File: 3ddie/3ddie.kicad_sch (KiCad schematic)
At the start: 53 parts, among them J1 USB4105-GF-A, J2 TRS_MIDI_IN, J3 TRS_MIDI_OUT, U1 W25Q128JV, U2 RP2040, U3 MCP1702T-3302E_CB, U4 MGC3130-I/MQ, U5 MCP1416R, U6 6N137, U7 BoostedElectrodes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

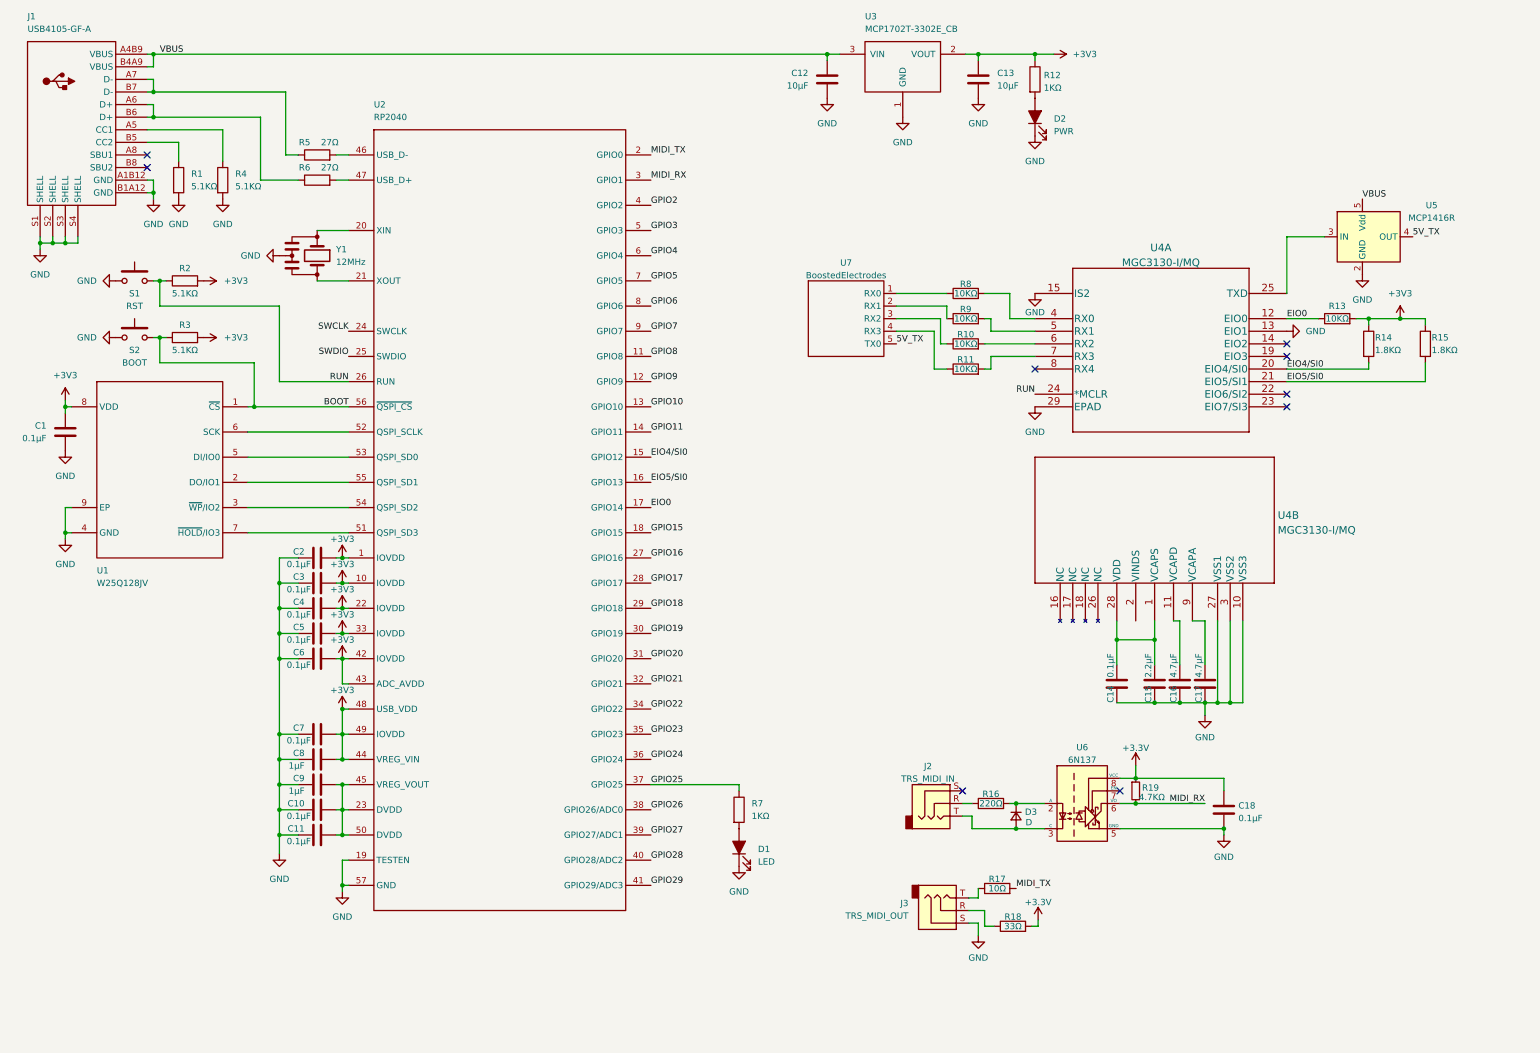
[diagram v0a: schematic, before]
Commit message: add datasheet links, part numbers, and catalog numbers to symbols
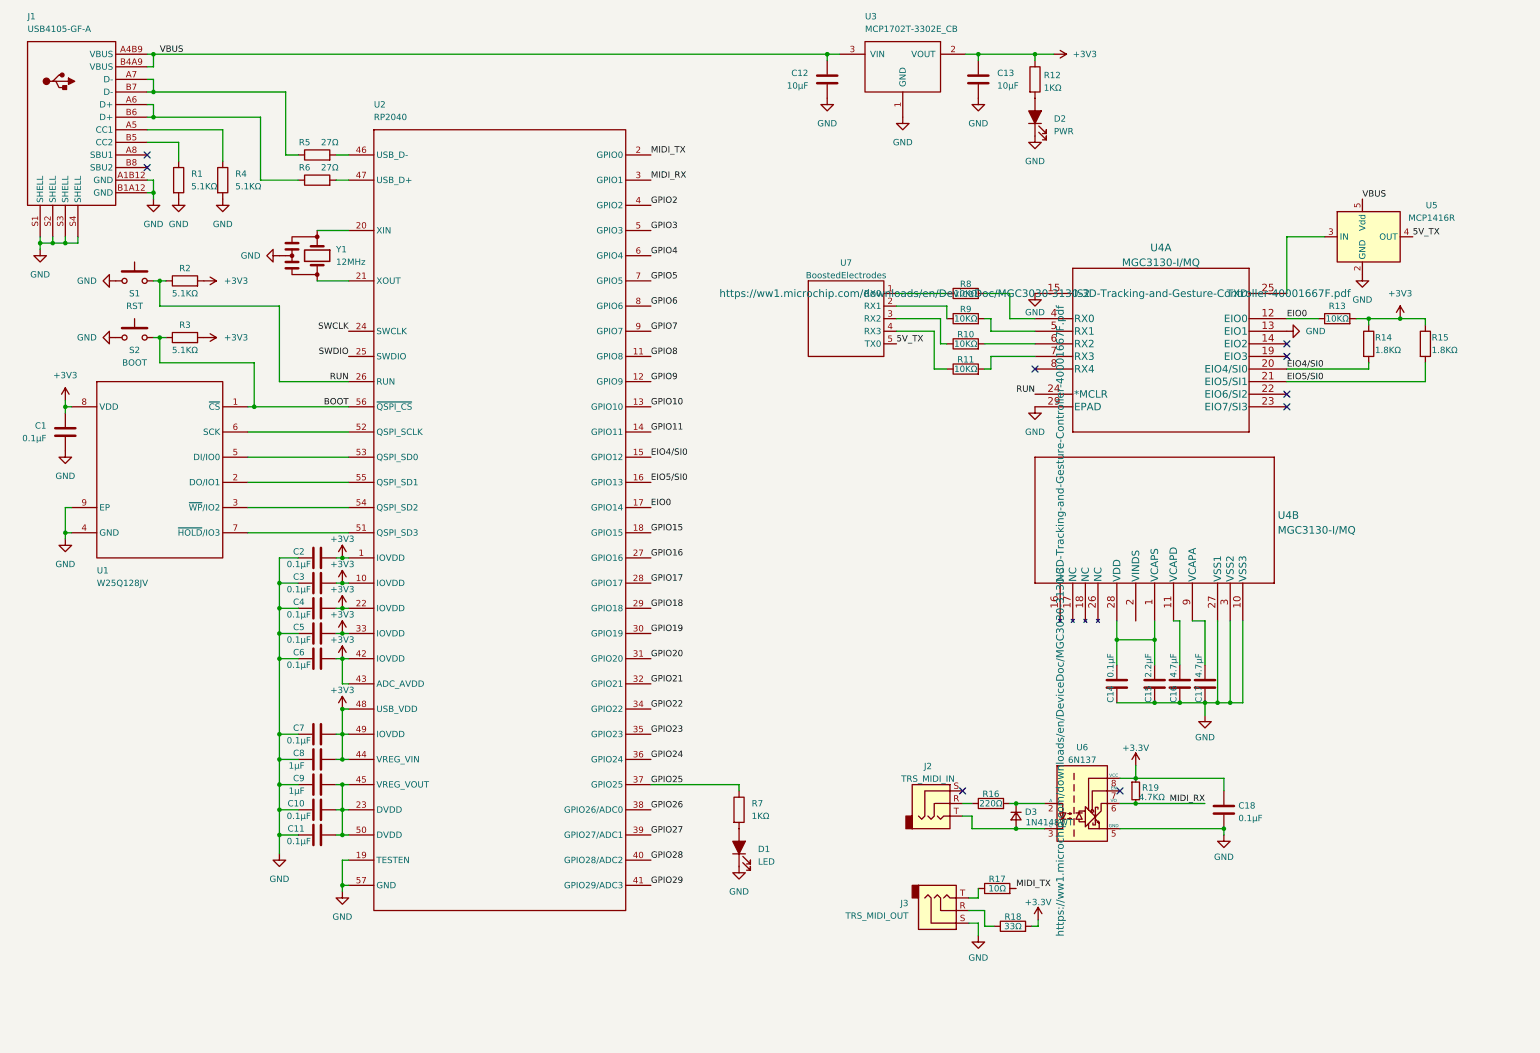
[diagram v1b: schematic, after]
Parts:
- D1: Digikey Catalog # (none) -> 160-1887-1-ND
- D2: Digikey Catalog # (none) -> 160-1427-1-ND
- D3: value D -> 1N4148WT; Digikey Catalog # (none) -> 1N4148WTCT-ND; Manufacturer Part # (none) -> 1N4148WT
- J1: Digikey Catalog # (none) -> 2073-USB4105-GF-ACT-ND; Manufacturer Part # (none) -> USB4105-GF-A
- S1, S2: Digikey Catalog # (none) -> CKN10778CT-ND; Manufacturer Part # (none) -> KTX 321 LHS
- U1: Digikey Catalog # (none) -> W25Q128JVPIMCT-ND; Manufacturer Part # (none) -> W25Q128JVPIM TR
- U2: Digikey Catalog # (none) -> 2648-SC0914(13)CT-ND; Manufacturer Part # (none) -> SC0914(13)
- U3: Digikey Catalog # (none) -> MCP1702T-3302E/CBCT-ND; Manufacturer Part # (none) -> MCP1702T-3302E/CB
- U4: Digikey Catalog # (none) -> MGC3130-I/MQ-ND; Manufacturer Part # (none) -> MGC3130-I/MQ
- U5: Digikey Catalog # (none) -> MCP1416RT-E/OTCT-ND; Manufacturer Part # (none) -> MCP1416RT-E/OT
- U6: footprint Package_DIP:DIP-8_W7.62mm -> (none); Digikey Catalog # (none) -> 6N137SM-ND; Manufacturer Part # (none) -> 6N137SM
- Y1: Digikey Catalog # (none) -> 490-17944-1-ND; Manufacturer Part # (none) -> CSTNE12M0G55A000R0
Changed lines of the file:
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@@
+      (effects (font (size 1.27 1.27)) hide)
+    )
+    (property "Digikey Catalog #" "MCP1416RT-E/OTCT-ND" (id 4) (at 292.1 66.04 0)
+      (effects (font (size 1.27 1.27)) hide)
+    )
+    (property "Manufacturer Part #" "MCP1416RT-E/OT" (id 5) (at 292.1 66.04 0)
       (effects (font (size 1.27 1.27)) hide)
     )
@@
       (effects (font (size 1.27 1.27)) hide)
     )
+    (property "Digikey Catalog #" "160-1887-1-ND" (id 4) (at 166.37 189.23 0)
+      (effects (font (size 1.27 1.27)) hide)
+    )
     (pin "1")
     (pin "2")
@@
       (effects (font (size 1.524 1.524)) hide)
     )
-    (property "Datasheet" "" (id 3) (at 231.14 143.51 0)
+    (property "Datasheet" "https://ww1.microchip.com/downloads/en/DeviceDoc/MGC3030-3130-3D-Tracking-and-Gesture-Controller-40001667F.pdf" (id 3) (at 231.14 143.51 0)
       (effects (font (size 1.524 1.524)))
+    )
+    (property "Digikey Catalog #" "MGC3130-I/MQ-ND" (id 4) (at 231.14 143.51 0)
+      (effects (font (size 1.27 1.27)) hide)
+    )
+    (property "Manufacturer Part #" "MGC3130-I/MQ" (id 5) (at 231.14 143.51 0)
+      (effects (font (size 1.27 1.27)) hide)
     )
     (pin "12")
@@
       (effects (font (size 1.27 1.27)) hide)
     )
-    (property "Datasheet" "" (id 3) (at 81.28 69.85 0)
+    (property "Datasheet" "https://www.murata.com/en/products/productdata/8801162002462/SPEC-CSTNE12M0G55A000R0.pdf" (id 3) (at 81.28 69.85 0)
+      (effects (font (size 1.27 1.27)) hide)
+    )
+    (property "Digikey Catalog #" "490-17944-1-ND" (id 4) (at 81.28 69.85 0)
+      (effects (font (size 1.27 1.27)) hide)
+    )
+    (property "Manufacturer Part #" "CSTNE12M0G55A000R0" (id 5) (at 81.28 69.85 0)
       (effects (font (size 1.27 1.27)) hide)
     )
@@
       (effects (font (size 1.524 1.524)) hide)
     )
-    (property "Datasheet" "" (id 3) (at 46.99 76.2 90)
+    (property "Datasheet" "https://www.ckswitches.com/media/1465/kxt3.pdf" (id 3) (at 46.99 76.2 90)
       (effects (font (size 1.524 1.524)) hide)
     )
+    (property "Digikey Catalog #" "CKN10778CT-ND" (id 4) (at 44.45 74.93 0)
+      (effects (font (size 1.27 1.27)) hide)
+    )
+    (property "Manufacturer Part #" "KTX 321 LHS" (id 5) (at 44.45 74.93 0)
+      (effects (font (size 1.27 1.27)) hide)
+    )
     (pin "1")
     (pin "2")
@@
       (effects (font (size 1.27 1.27)) (justify left))
     )
-    (property "Value" "D" (id 1) (at 224.155 184.15 90)
+    (property "Value" "1N4148WT" (id 1) (at 224.155 184.15 90)
       (effects (font (size 1.27 1.27)) (justify left))
     )
@@
       (effects (font (size 1.27 1.27)) hide)
     )
-    (property "Datasheet" "~" (id 3) (at 222.25 182.88 90)
+    (property "Datasheet" "https://rocelec.widen.net/view/pdf/bnxdzepaue/ONSM-S-A0003584797-1.pdf?t.download=true&u=5oefqw" (id 3) (at 222.25 182.88 90)
+      (effects (font (size 1.27 1.27)) hide)
+    )
+    (property "Digikey Catalog #" "1N4148WTCT-ND" (id 4) (at 222.25 182.88 0)
+      (effects (font (size 1.27 1.27)) hide)
+    )
+    (property "Manufacturer Part #" "1N4148WT" (id 5) (at 222.25 182.88 0)
       (effects (font (size 1.27 1.27)) hide)
     )
@@
       (effects (font (size 1.524 1.524)) hide)
     )
-    (property "Datasheet" "" (id 3) (at 46.99 87.63 90)
+    (property "Datasheet" "https://www.ckswitches.com/media/1465/kxt3.pdf" (id 3) (at 46.99 87.63 90)
       (effects (font (size 1.524 1.524)) hide)
+    )
+    (property "Digikey Catalog #" "CKN10778CT-ND" (id 4) (at 44.45 86.36 0)
+      (effects (font (size 1.27 1.27)) hide)
+    )
+    (property "Manufacturer Part #" "KTX 321 LHS" (id 5) (at 44.45 86.36 0)
+      (effects (font (size 1.27 1.27)) hide)
     )
     (pin "1")
@@
       (effects (font (size 1.524 1.524)) hide)
     )
-    (property "Datasheet" "" (id 3) (at 226.06 77.47 0)
+    (property "Datasheet" "https://ww1.microchip.com/downloads/en/DeviceDoc/MGC3030-3130-3D-Tracking-and-Gesture-Controller-40001667F.pdf" (id 3) (at 226.06 77.47 0)
       (effects (font (size 1.524 1.524)))
+    )
+    (property "Digikey Catalog #" "MGC3130-I/MQ-ND" (id 4) (at 226.06 77.47 0)
+      (effects (font (size 1.27 1.27)) hide)
+    )
+    (property "Manufacturer Part #" "MGC3130-I/MQ" (id 5) (at 226.06 77.47 0)
+      (effects (font (size 1.27 1.27)) hide)
     )
     (pin "12")
@@
     (property "Reference" "U6" (id 0) (at 235.585 169.0202 0))
     (property "Value" "6N137" (id 1) (at 235.585 171.5571 0))
-    (property "Footprint" "Package_DIP:DIP-8_W7.62mm" (id 2) (at 235.585 193.04 0)
-      (effects (font (size 1.27 1.27)) hide)
-    )
-    (property "Datasheet" "https://docs.broadcom.com/docs/AV02-0940EN" (id 3) (at 213.995 166.37 0)
+    (property "Footprint" "" (id 2) (at 235.585 193.04 0)
+      (effects (font (size 1.27 1.27)) hide)
+    )
+    (property "Datasheet" "https://rocelec.widen.net/view/pdf/zs07d29frw/ONSM-S-A0003591003-1.pdf?t.download=true&u=5oefqw" (id 3) (at 213.995 166.37 0)
+      (effects (font (size 1.27 1.27)) hide)
+    )
+    (property "Digikey Catalog #" "6N137SM-ND" (id 4) (at 235.585 180.34 0)
+      (effects (font (size 1.27 1.27)) hide)
+    )
+    (property "Manufacturer Part #" "6N137SM" (id 5) (at 235.585 180.34 0)
       (effects (font (size 1.27 1.27)) hide)
     )
@@
       (effects (font (size 1.27 1.27)) hide)
     )
+    (property "Digikey Catalog #" "160-1427-1-ND" (id 4) (at 226.06 41.91 0)
+      (effects (font (size 1.27 1.27)) hide)
+    )
     (pin "1")
     (pin "2")
@@
       (effects (font (size 1.524 1.524)) hide)
     )
-    (property "Datasheet" "" (id 3) (at 199.39 30.48 0)
+    (property "Datasheet" "https://ww1.microchip.com/downloads/en/DeviceDoc/22008E.pdf" (id 3) (at 199.39 30.48 0)
       (effects (font (size 1.524 1.524)) hide)
     )
+    (property "Digikey Catalog #" "MCP1702T-3302E/CBCT-ND" (id 4) (at 199.39 31.75 0)
+      (effects (font (size 1.27 1.27)) hide)
+    )
+    (property "Manufacturer Part #" "MCP1702T-3302E/CB" (id 5) (at 199.39 31.75 0)
+      (effects (font (size 1.27 1.27)) hide)
+    )
     (pin "1")
     (pin "2")
@@
     )
     (property "Datasheet" "" (id 3) (at 29.21 39.37 0)
+      (effects (font (size 1.27 1.27)) hide)
+    )
+    (property "Digikey Catalog #" "2073-USB4105-GF-ACT-ND" (id 4) (at 31.75 43.18 0)
+      (effects (font (size 1.27 1.27)) hide)
+    )
+    (property "Manufacturer Part #" "USB4105-GF-A" (id 5) (at 31.75 43.18 0)
       (effects (font (size 1.27 1.27)) hide)
     )
@@
       (effects (font (size 1.27 1.27)) hide)
     )
-    (property "Datasheet" "" (id 3) (at 54.61 104.14 0)
+    (property "Datasheet" "https://www.winbond.com/resource-files/w25q128jv_dtr%20revc%2003272018%20plus.pdf" (id 3) (at 54.61 104.14 0)
+      (effects (font (size 1.27 1.27)) hide)
+    )
+    (property "Digikey Catalog #" "W25Q128JVPIMCT-ND" (id 4) (at 49.53 113.03 0)
+      (effects (font (size 1.27 1.27)) hide)
+    )
+    (property "Manufacturer Part #" "W25Q128JVPIM TR" (id 5) (at 49.53 113.03 0)
       (effects (font (size 1.27 1.27)) hide)
     )
@@
       (effects (font (size 1.27 1.27)) hide)
     )
-    (property "Datasheet" "" (id 3) (at 124.46 87.63 0)
+    (property "Datasheet" "https://datasheets.raspberrypi.com/rp2040/rp2040-datasheet.pdf" (id 3) (at 124.46 87.63 0)
+      (effects (font (size 1.27 1.27)) hide)
+    )
+    (property "Digikey Catalog #" "2648-SC0914(13)CT-ND" (id 4) (at 118.11 123.19 0)
+      (effects (font (size 1.27 1.27)) hide)
+    )
+    (property "Manufacturer Part #" "SC0914(13)" (id 5) (at 118.11 123.19 0)
       (effects (font (size 1.27 1.27)) hide)
     )
@@
     )
     (path "/6c8f9fa6-c3d2-4a4b-a5e3-d21e80be9063"
-      (reference "D3") (unit 1) (value "D") (footprint "")
+      (reference "D3") (unit 1) (value "1N4148WT") (footprint "")
     )
     (path "/e852571c-5d4c-418a-a34d-71f60de57e95"
@@
     )
     (path "/bca2ac86-8d9c-4b32-ab1d-2258827622a1"
-      (reference "U6") (unit 1) (value "6N137") (footprint "Package_DIP:DIP-8_W7.62mm")
+      (reference "U6") (unit 1) (value "6N137") (footprint "")
     )
     (path "/0030390e-c97e-47e6-97d2-f7c983a931fc"

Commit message: specify optocoupler diode, assign some footprints
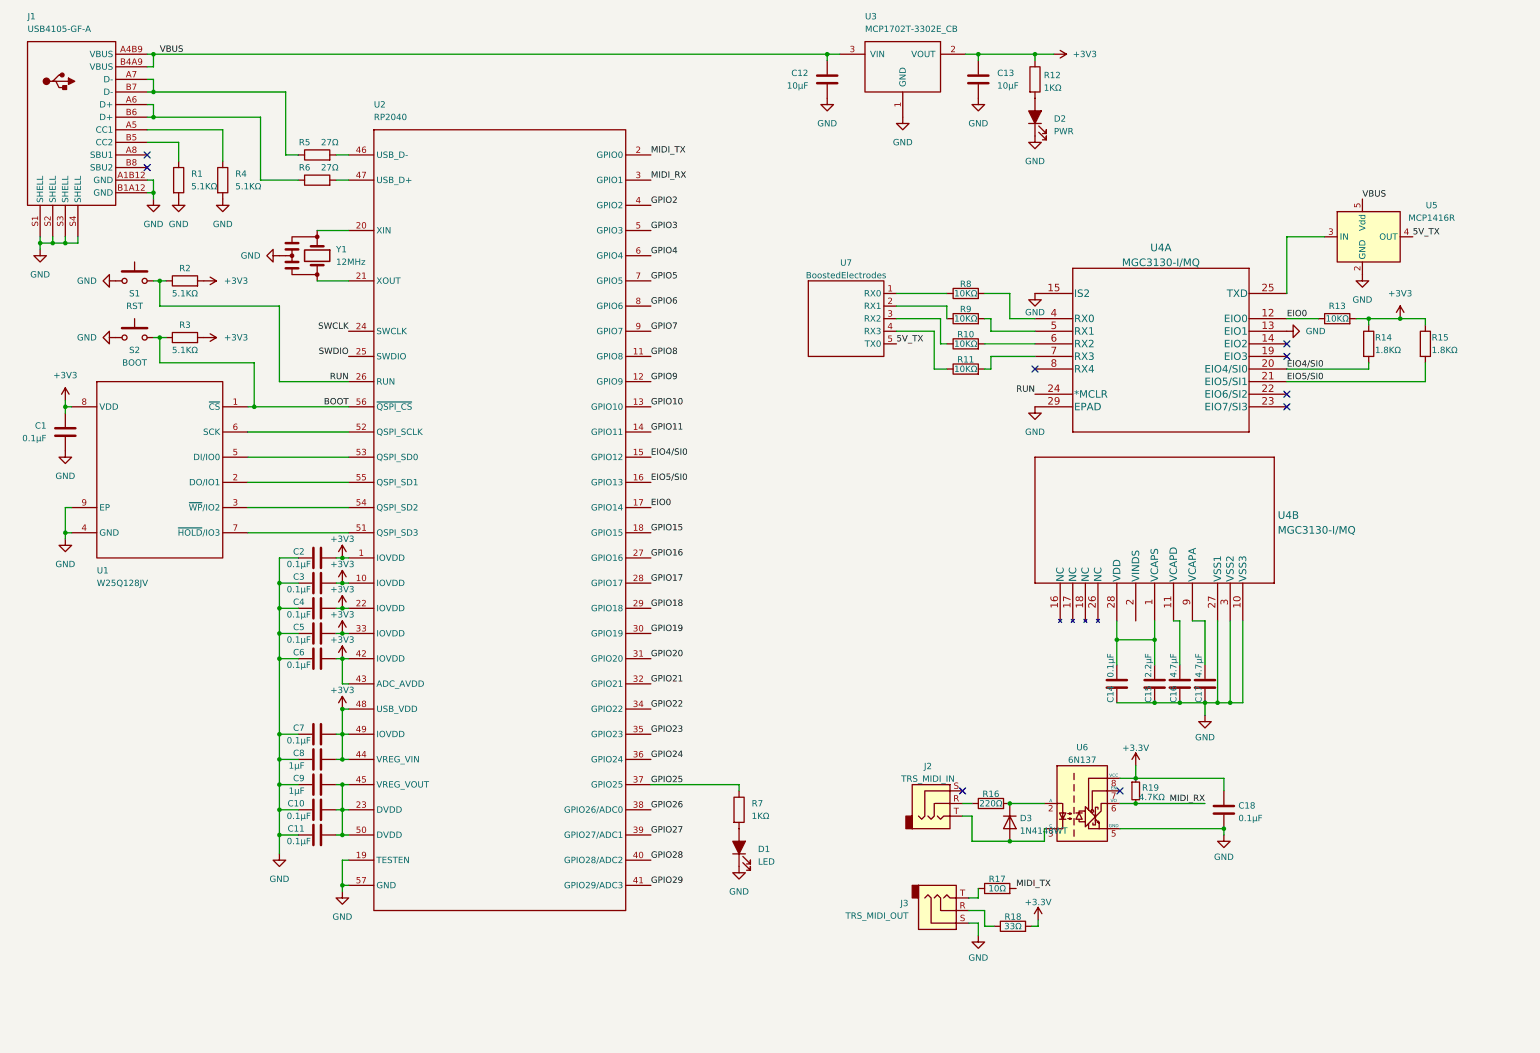
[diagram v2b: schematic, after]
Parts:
- removed D3: 1N4148WT, symbol Device:D_Small
- added D3: 1N4148WT, Diode_SMD:D_SOD-523, symbol Diode:1N4148WT
- C14, C15, C18: footprint (none) -> Capacitor_SMD:C_0402_1005Metric
- C16, C17: footprint (none) -> Capacitor_SMD:C_0603_1608Metric
- R10, R11, R13, R14, R15, R16, R17, R18, R19, R8, R9: footprint (none) -> Resistor_SMD:R_0402_1005Metric
- U4: footprint QFN28_5X5MQ_MCH -> (none)
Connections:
- net at J2.T, U6.3 (C): now also D3.2 (A)
- net at R16.2, U6.2 (A): now also D3.1 (K)
